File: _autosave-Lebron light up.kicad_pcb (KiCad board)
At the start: 2 copper layers, 141 x 105.1 mm, 16 parts, among them M1 Motor_DC, SW1 SW_Push

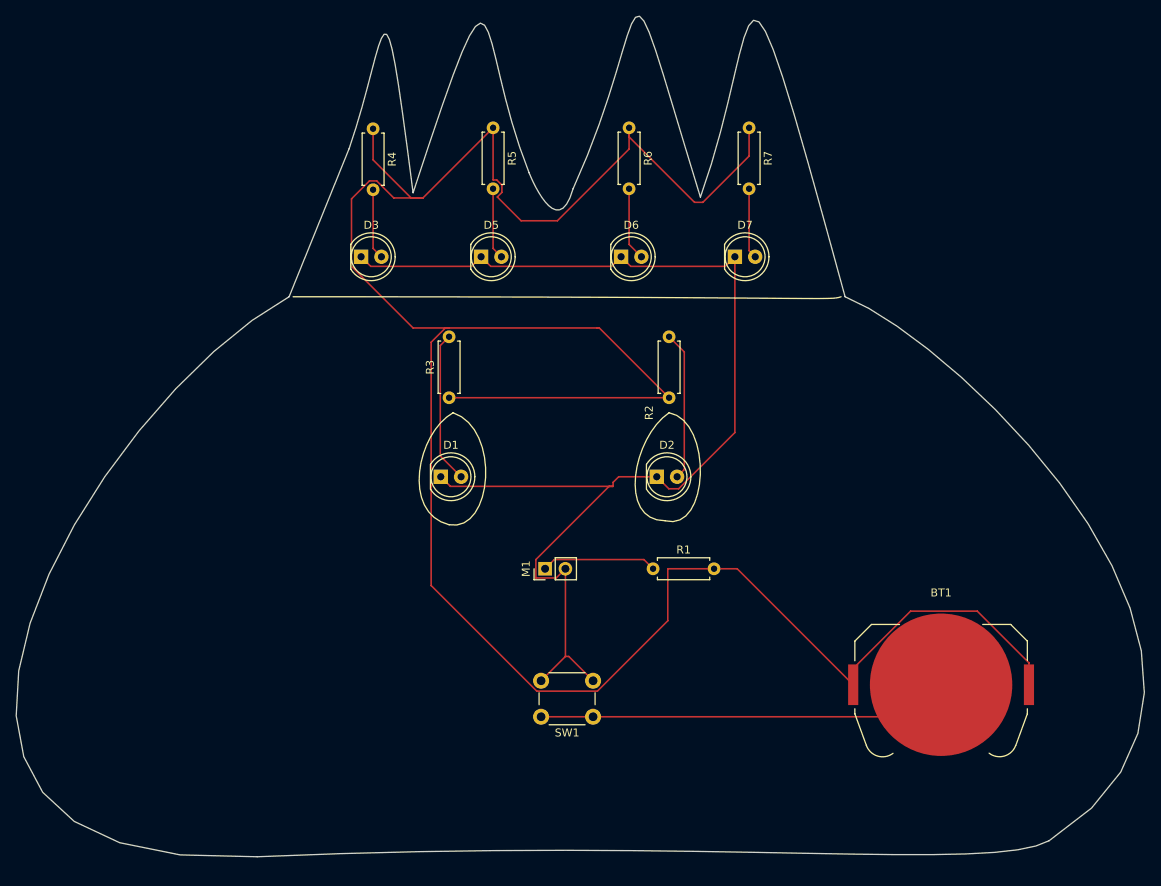
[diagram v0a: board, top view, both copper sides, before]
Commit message: Recreated the Desgin to make it smaller and add a image.
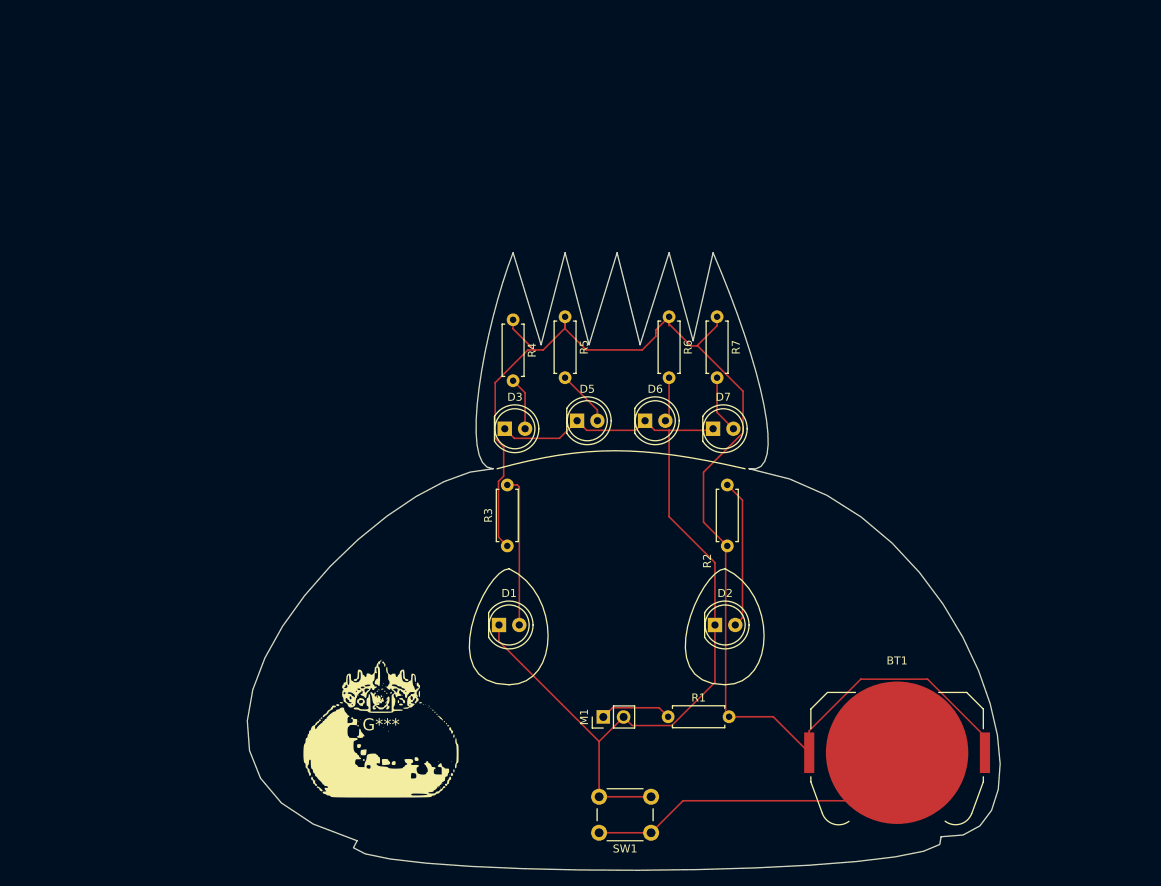
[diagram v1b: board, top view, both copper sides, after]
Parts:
- added G***: LOGO, LOGO, F.Cu at (114.5, 114.0)
- moved R4 29.6 mm to (131.0, 63.4)
- moved D3 28.0 mm to (130.0, 77.0)
- moved R5 25.3 mm to (137.5, 63.0)
- moved R6 24.1 mm to (150.5, 63.0)
- moved R7 24.0 mm to (156.5, 63.0)
- moved D5 23.8 mm to (139.0, 76.0)
- moved D7 21.7 mm to (156.0, 77.0)
- moved D6 20.7 mm to (147.5, 76.0)
- moved D1 19.9 mm to (129.2, 101.5)
- moved D2 19.9 mm to (156.2, 101.5)
- moved M1 19.9 mm to (142.3, 113.0)
- moved R2 19.9 mm to (157.8, 91.6)
- moved R3 19.9 mm to (130.3, 91.6)
- moved R1 18.6 mm to (150.4, 113.0)
- moved SW1 16.2 mm to (148.2, 127.5)
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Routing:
- net Net-(BT1-+): track 317.0 -> 165.1 mm
- net Net-(D1-K): track 153.2 -> 114.5 mm
- net Net-(BT1--): track 51.7 -> 41.4 mm
- net Net-(M1-+): track 14.5 -> 9.07 mm
- net Net-(D6-A): track 9.14 -> 5.57 mm
- net Net-(D3-A): track 8.81 -> 6.62 mm
- net Net-(D5-A): track 8.93 -> 7.05 mm
- net Net-(D7-A): track 8.82 -> 7.22 mm
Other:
- board size 141 x 105.1 mm -> 94.1 x 77.2 mm

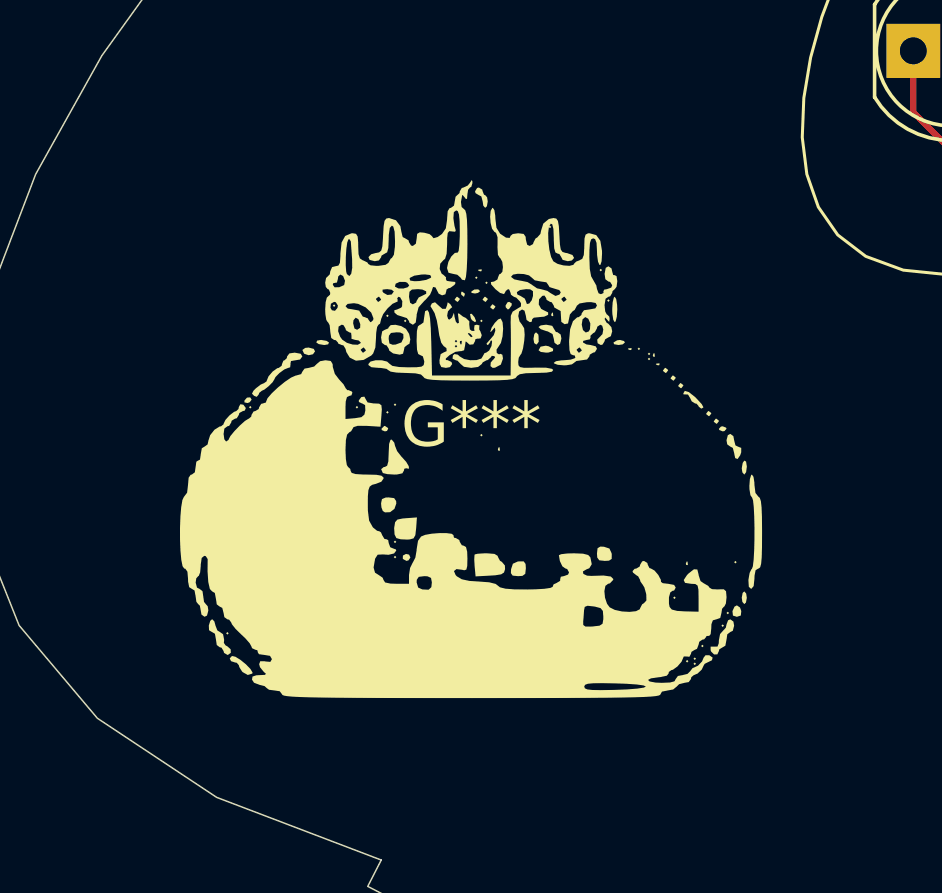
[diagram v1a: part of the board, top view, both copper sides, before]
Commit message: Fixed the crown by removing the pointy edges
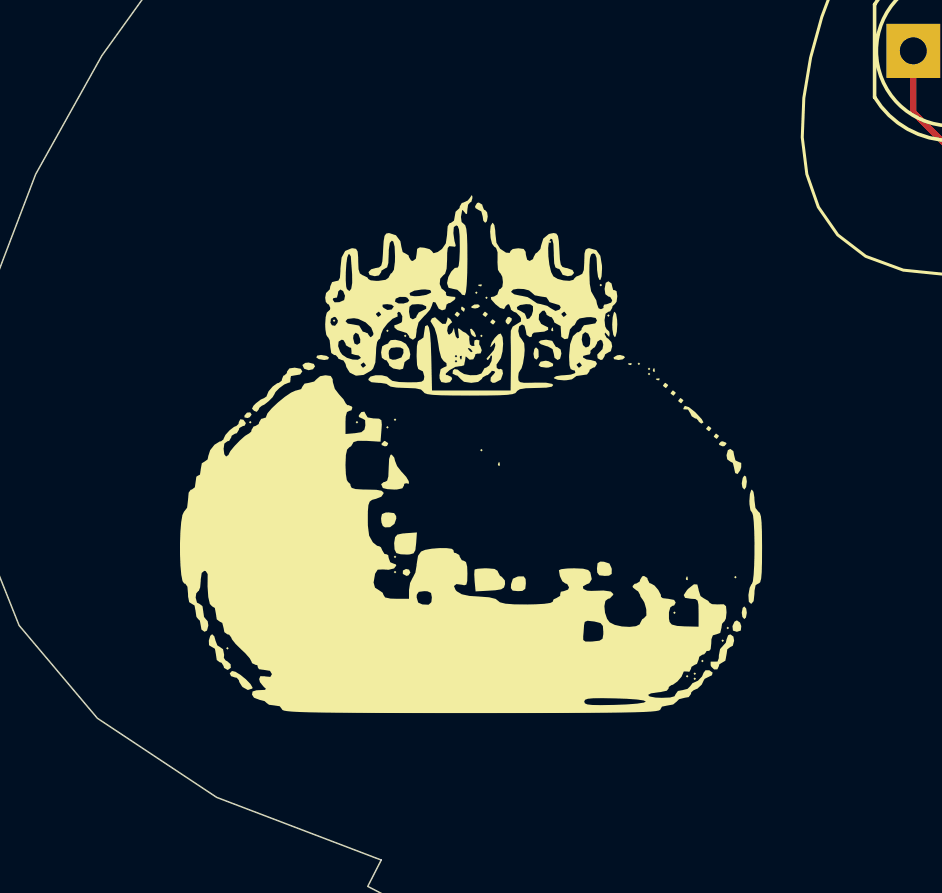
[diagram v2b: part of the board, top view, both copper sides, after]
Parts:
- moved G*** 0.50 mm to (114.5, 114.5)
